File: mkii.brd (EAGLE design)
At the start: 47.8 x 29 mm, 52 parts, among them IC1 ATMEGA32U2, Q1 16MHz, U1 GTL2003, U2 TS1117, U3 PRTR5V0U2AX, X1 MINI-USB-32005-301

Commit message: 22p cap for crystal
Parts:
- C1, C2: value 33p -> 22p
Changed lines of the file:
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@@
 <attribute name="OC_FARNELL" value="1667008" x="12.954" y="20.701" size="1.778" layer="27" rot="R270" display="off"/>
 </element>
-<element name="C1" library="rcl" package="C0603" value="33p" x="15.494" y="19.431" smashed="yes" rot="MR0">
+<element name="C1" library="rcl" package="C0603" value="22p" x="15.494" y="19.431" smashed="yes" rot="MR0">
 <attribute name="NAME" x="16.891" y="19.939" size="1.016" layer="26" rot="MR180"/>
 <attribute name="VALUE" x="16.51" y="20.32" size="1.27" layer="28" rot="MR180"/>
 </element>
-<element name="C2" library="rcl" package="C0603" value="33p" x="15.494" y="21.971" smashed="yes" rot="MR0">
+<element name="C2" library="rcl" package="C0603" value="22p" x="15.494" y="21.971" smashed="yes" rot="MR0">
 <attribute name="NAME" x="16.891" y="22.479" size="1.016" layer="26" rot="MR180"/>
 <attribute name="VALUE" x="16.51" y="22.86" size="1.27" layer="28" rot="MR180"/>

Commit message: pin4 on usb is id, pin5 is gnd. upstream idiots.
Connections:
- net GND: now also X1.5; no longer X1.4
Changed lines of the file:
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@@
 <setting verticaltext="up"/>
 </settings>
-<grid distance="0.635" unitdist="mm" unit="mm" style="lines" multiple="1" display="yes" altdistance="5" altunitdist="mil" altunit="mic"/>
+<grid distance="0.635" unitdist="mm" unit="mm" style="lines" multiple="1" display="yes" altdistance="0.127" altunitdist="mm" altunit="mm"/>
 <layers>
 <layer number="1" name="Top" color="4" fill="1" visible="yes" active="yes"/>
@@
 <layer number="27" name="tValues" color="7" fill="1" visible="no" active="yes"/>
 <layer number="28" name="bValues" color="7" fill="1" visible="no" active="yes"/>
-<layer number="29" name="tStop" color="7" fill="3" visible="no" active="yes"/>
+<layer number="29" name="tStop" color="7" fill="3" visible="yes" active="yes"/>
 <layer number="30" name="bStop" color="7" fill="6" visible="no" active="yes"/>
 <layer number="31" name="tCream" color="7" fill="4" visible="no" active="yes"/>
@@
 <contactref element="RST" pad="1"/>
 <contactref element="C3" pad="1"/>
-<contactref element="X1" pad="4"/>
 <contactref element="LED1" pad="C"/>
 <contactref element="LED2" pad="C"/>
@@
 <contactref element="U3" pad="1"/>
 <contactref element="U3" pad="1"/>
+<contactref element="X1" pad="5"/>
 </signal>
 <signal name="VCC" class="1">

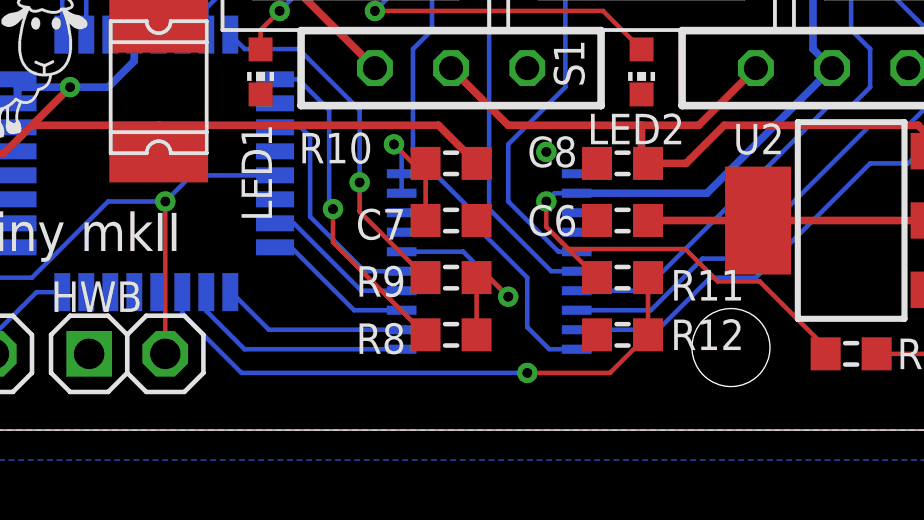
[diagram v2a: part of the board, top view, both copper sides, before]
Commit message: remote circuit on pb5
can't remember my thoughts – without ADC there is no vbus
detection.
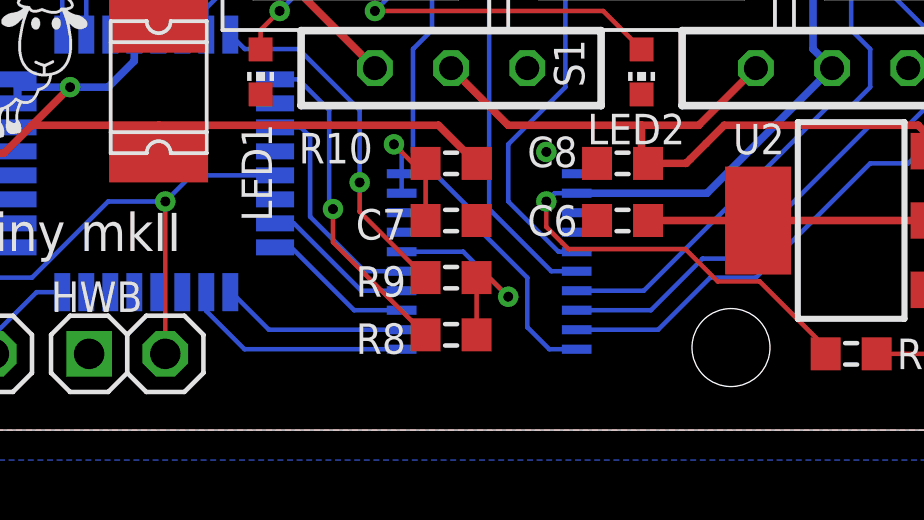
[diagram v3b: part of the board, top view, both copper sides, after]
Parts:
- removed R11, R12: 1M, rcl:R0603
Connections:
- removed net N$5: IC1.19, R11.2, R12.1
- net GND: no longer R12.2
- net V+: no longer R11.1
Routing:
- net N$5: track 19.5 -> 0.00 mm, vias 1 -> 0
- net V+: track 59.1 -> 57.7 mm
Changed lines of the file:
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@@
 <attribute name="VALUE" x="22.606" y="14.732" size="1.778" layer="21" ratio="10"/>
-</element>
-<element name="R11" library="rcl" package="R0603" value="1M" x="32.385" y="5.08" smashed="yes">
-<attribute name="NAME" x="36.449" y="5.334" size="1.016" layer="25" rot="R180"/>
-<attribute name="VALUE" x="31.75" y="5.715" size="1.27" layer="27" rot="R180"/>
-</element>
-<element name="R12" library="rcl" package="R0603" value="1M" x="32.385" y="3.175" smashed="yes" rot="R180">
-<attribute name="NAME" x="36.449" y="3.683" size="1.016" layer="25" rot="R180"/>
-<attribute name="VALUE" x="31.75" y="3.81" size="1.27" layer="27" rot="R180"/>
 </element>
 <element name="U$1" library="creative-commons" package="CC_TPLACE_HS" value="CC-TPLACE-HALF" x="40.3225" y="23.0505" rot="MR0"/>
@@
 <via x="17.78" y="17.145" extent="1-16" drill="0.3302"/>
 <via x="10.16" y="13.335" extent="1-16" drill="0.3302"/>
-<contactref element="R12" pad="2"/>
 <via x="45.085" y="5.715" extent="1-16" drill="0.3302"/>
 <contactref element="U3" pad="1"/>
 <contactref element="U3" pad="1"/>
 <contactref element="X1" pad="5"/>
+<wire x1="45.72" y1="12.688" x2="43.815" y2="18.415" width="0" layer="19" extent="1-1"/>
+<wire x1="45.085" y1="5.715" x2="45.72" y2="12.688" width="0" layer="19" extent="1-1"/>
+<wire x1="43.104" y1="4.674" x2="45.085" y2="5.715" width="0" layer="19" extent="1-1"/>
+<wire x1="34.29" y1="18.415" x2="43.815" y2="18.415" width="0" layer="19" extent="1-1"/>
+<wire x1="33.02" y1="11.188" x2="34.29" y2="18.415" width="0" layer="19" extent="1-1"/>
+<wire x1="31.535" y1="8.89" x2="33.02" y2="11.188" width="0" layer="19" extent="1-1"/>
+<wire x1="30.8578" y1="8.545" x2="31.535" y2="8.89" width="0" layer="19" extent="1-16"/>
+<wire x1="29.845" y1="9.271" x2="30.8578" y2="8.545" width="0" layer="19" extent="16-16"/>
+<wire x1="31.535" y1="6.985" x2="30.8578" y2="8.545" width="0" layer="19" extent="1-16"/>
+<wire x1="27.52" y1="6.985" x2="29.845" y2="9.271" width="0" layer="19" extent="1-1"/>
+<wire x1="20.32" y1="11.188" x2="27.52" y2="6.985" width="0" layer="19" extent="1-1"/>
+<wire x1="15.31" y1="13.1826" x2="20.32" y2="11.188" width="0" layer="19" extent="1-16"/>
+<wire x1="15.66" y1="15.24" x2="15.31" y2="13.1826" width="0" layer="19" extent="16-16"/>
+<wire x1="15.24" y1="17.78" x2="15.66" y2="15.24" width="0" layer="19" extent="16-16"/>
+<wire x1="16.344" y1="19.431" x2="15.24" y2="17.78" width="0" layer="19" extent="16-16"/>
+<wire x1="16.344" y1="21.971" x2="16.344" y2="19.431" width="0" layer="19" extent="16-16"/>
+<wire x1="17.78" y1="17.145" x2="15.24" y2="17.78" width="0" layer="19" extent="1-1"/>
+<wire x1="10.16" y1="13.335" x2="15.31" y2="13.1826" width="0" layer="19" extent="16-16"/>
+<wire x1="9.355" y1="17.895" x2="10.16" y2="13.335" width="0" layer="19" extent="16-16"/>
+<wire x1="8.255" y1="19.685" x2="9.355" y2="17.895" width="0" layer="19" extent="16-16"/>
+<wire x1="7.445" y1="20.625" x2="8.255" y2="19.685" width="0" layer="19" extent="1-1"/>
+<wire x1="6.35" y1="19.685" x2="7.445" y2="20.625" width="0" layer="19" extent="1-1"/>
+<wire x1="12.2174" y1="8.49" x2="10.16" y2="13.335" width="0" layer="19" extent="16-16"/>
+<wire x1="7.94" y1="8.255" x2="12.2174" y2="8.49" width="0" layer="19" extent="16-16"/>
+<wire x1="4.445" y1="13.63" x2="10.16" y2="13.335" width="0" layer="19" extent="1-1"/>
+<wire x1="8.89" y1="2.54" x2="7.94" y2="8.255" width="0" layer="19" extent="16-16"/>
+<wire x1="14.605" y1="2.54" x2="8.89" y2="2.54" width="0" layer="19" extent="1-1"/>
+<wire x1="24.765" y1="18.415" x2="17.78" y2="17.145" width="0" layer="19" extent="1-1"/>
 </signal>
 <signal name="VCC" class="1">
@@
 <contactref element="SV1" pad="2"/>
 <contactref element="SV2" pad="2"/>
-<contactref element="R11" pad="1"/>
 <wire x1="39.37" y1="12.065" x2="35.2" y2="7.895" width="0.254" layer="16"/>
 <wire x1="30.8578" y1="7.895" x2="35.2" y2="7.895" width="0.254" layer="16"/>
@@
 <wire x1="39.37" y1="12.065" x2="38.735" y2="12.7" width="0.254" layer="16"/>
 <wire x1="38.735" y1="12.7" x2="38.735" y2="24.765" width="0.254" layer="16"/>
-<wire x1="31.535" y1="5.08" x2="30.5825" y2="6.0325" width="0.1524" layer="1"/>
 <wire x1="30.3725" y1="6.2425" x2="29.845" y2="6.77" width="0.1524" layer="1"/>
 <wire x1="29.845" y1="6.77" x2="29.845" y2="7.62" width="0.1524" layer="1"/>
@@
 <wire x1="19.685" y1="15.24" x2="20.105" y2="15.24" width="0.1524" layer="16"/>
 </signal>
-<signal name="N$5">
-<contactref element="IC1" pad="19"/>
-<contactref element="R11" pad="2"/>
-<contactref element="R12" pad="1"/>
-<wire x1="17.71" y1="4.5974" x2="17.71" y2="3.88" width="0.1524" layer="16"/>
-<wire x1="17.71" y1="3.88" x2="19.685" y2="1.905" width="0.1524" layer="16"/>
-<wire x1="19.685" y1="1.905" x2="29.21" y2="1.905" width="0.1524" layer="16"/>
-<via x="29.21" y="1.905" extent="1-16" drill="0.3302"/>
-<wire x1="33.235" y1="3.175" x2="33.235" y2="5.08" width="0.1524" layer="1"/>
-<wire x1="33.235" y1="3.175" x2="31.965" y2="1.905" width="0.1524" layer="1"/>
-<wire x1="31.965" y1="1.905" x2="29.21" y2="1.905" width="0.1524" layer="1"/>
-</signal>
 <signal name="N$6" class="1">

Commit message: unknown changes
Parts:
- C6, C8: device rcl:C0603 -> rcl:C0805
- moved C6 0.51 mm to (32.4, 6.48)
- moved C8 0.25 mm to (32.4, 8.64)
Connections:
- removed net N$23: C8.2, S1.C, S2.1, U2.3
- new net N$2: S1.2, S2.C
- net N$6: now also C8.2, S2.1, U2.3; no longer S1.2
- net V+: now also S1.C; no longer R7.2, S2.C
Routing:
- net N$6: track 9.21 -> 35.1 mm
- net N$23: track 23.9 -> 0.00 mm
- net N$25: track 28.9 -> 31.8 mm
- net V+: track 57.7 -> 56.7 mm
- net N$32: track 18.2 -> 17.4 mm
- net N$26: vias 1 -> 0
